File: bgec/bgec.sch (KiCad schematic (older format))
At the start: 7 parts

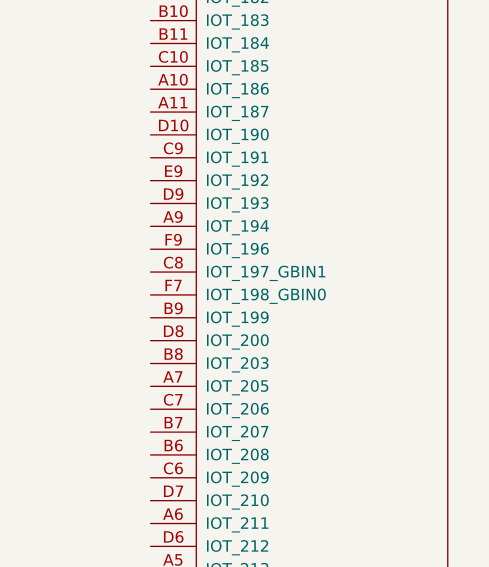
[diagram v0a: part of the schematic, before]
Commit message: Add clock and reset connections
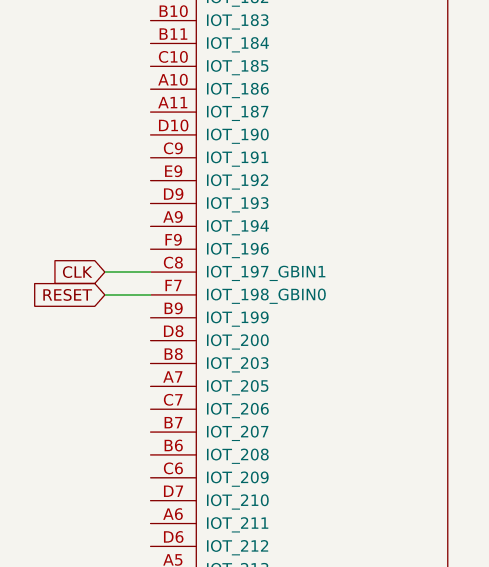
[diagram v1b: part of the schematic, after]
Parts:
- C1: footprint (none) -> Capacitor_SMD:C_0402_1005Metric
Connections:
- net CLK: now also FPGAiCE40HX1.C8 (IOT_197_GBIN1)
- net RESET: now reaches FPGAiCE40HX1.F7 (IOT_198_GBIN0)
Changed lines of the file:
@@
 F 0 "C1" V 7402 1100 50  0000 C CNN
 F 1 "100nF" V 7311 1100 50  0000 C CNN
-F 2 "" H 7188 950 50  0001 C CNN
+F 2 "Capacitor_SMD:C_0402_1005Metric" H 7188 950 50  0001 C CNN
 F 3 "~" H 7150 1100 50  0001 C CNN
 	1    7150 1100
@@
 Text GLabel 7500 1300 2    50   Input ~ 0
 GCLogicGround
+Text GLabel 800  4100 0    50   Input ~ 0
+RESET
+Text GLabel 800  4000 0    50   Input ~ 0
+CLK
+Wire Wire Line
+	800  4000 1000 4000
+Wire Wire Line
+	800  4100 1000 4100
 $EndSCHEMATC

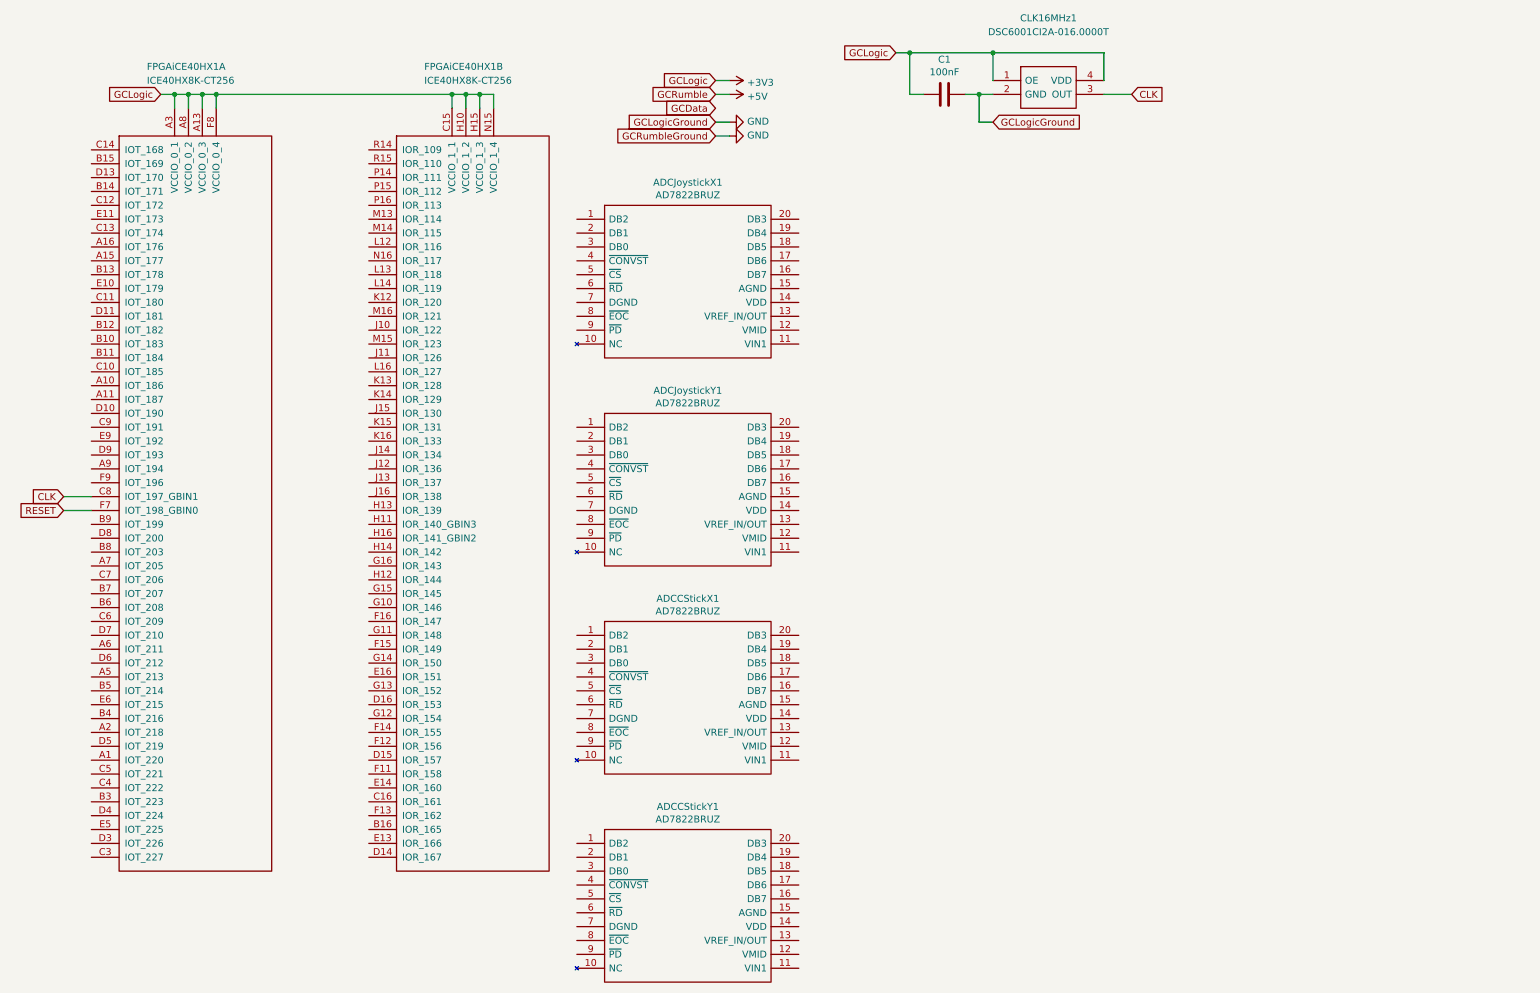
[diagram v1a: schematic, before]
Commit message: Connect the ADCs
I might be doing this wrong by ignoring CONVST. We'll see. I need to update the software side of things to start doing Parallel ADCs.
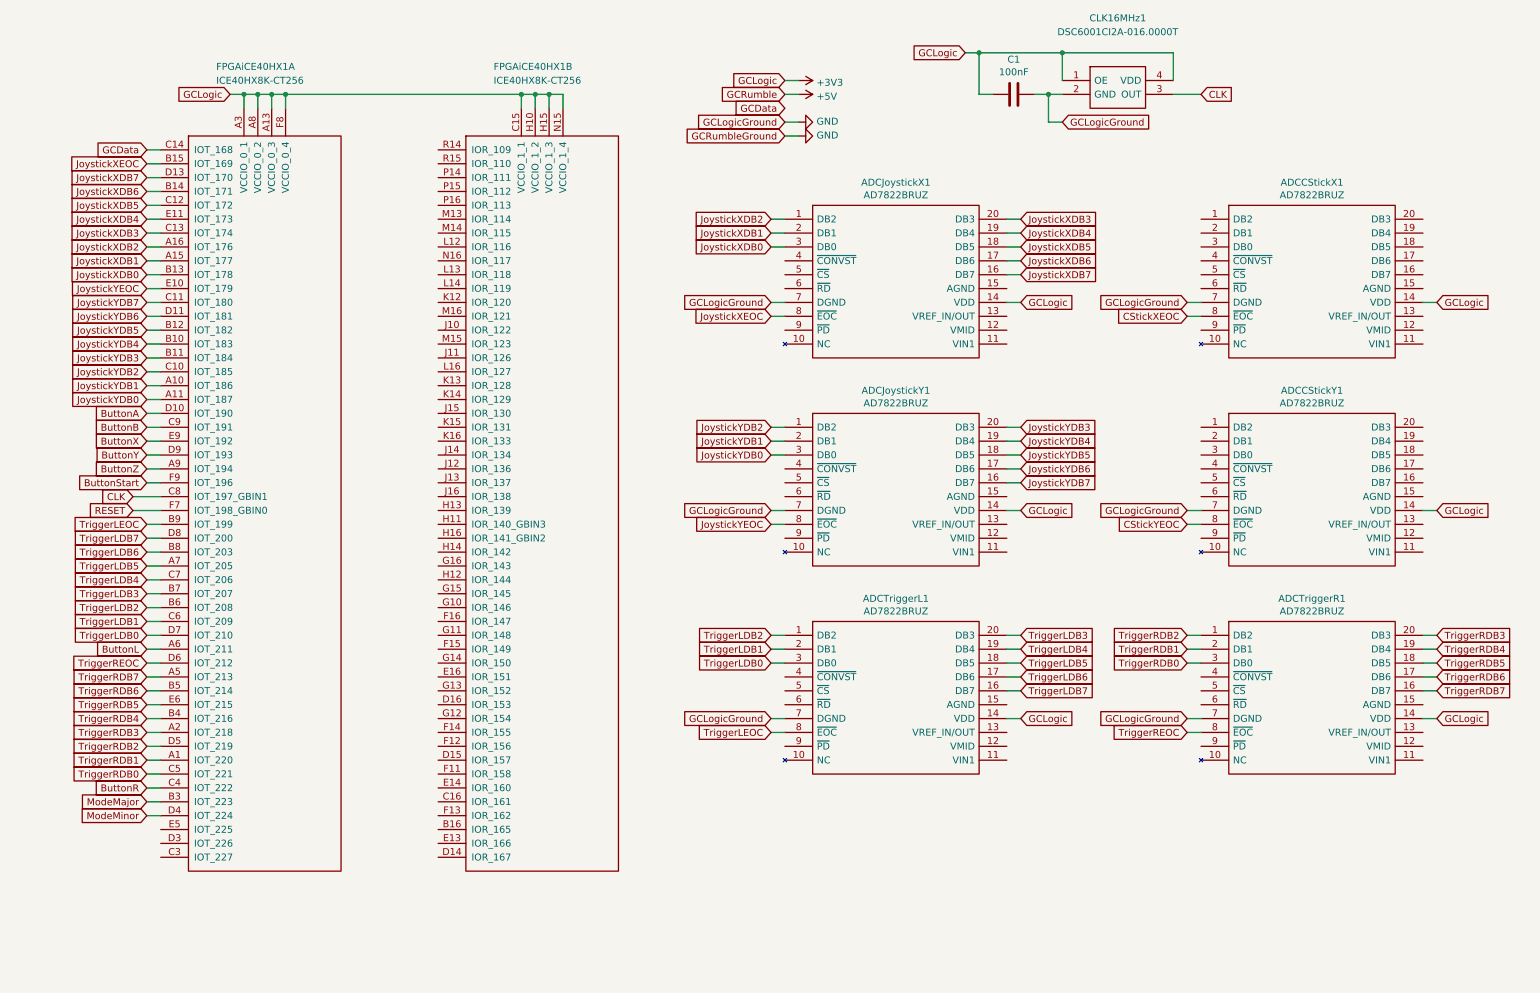
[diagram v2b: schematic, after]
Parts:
- added ADCTriggerL1, ADCTriggerR1: AD7822BRUZ, SOP65P640X120-20N, symbol bgec:AD7822BRUZ
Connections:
- net +3V3: now also ADCCStickX1.14 (VDD), ADCCStickY1.14 (VDD), ADCJoystickX1.14 (VDD), ADCJoystickY1.14 (VDD), ADCTriggerL1.14 (VDD), ADCTriggerR1.14 (VDD)
- net GCData: now also FPGAiCE40HX1.C14 (IOT_168)
- net GND: now also ADCCStickX1.7 (DGND), ADCCStickY1.7 (DGND), ADCJoystickX1.7 (DGND), ADCJoystickY1.7 (DGND), ADCTriggerL1.7 (DGND), ADCTriggerR1.7 (DGND)
- net JoystickXDB2: now reaches ADCJoystickX1.1 (DB2)
- net JoystickXDB2: now also FPGAiCE40HX1.A16 (IOT_176)
- net JoystickXDB7: now reaches ADCJoystickX1.16 (DB7)
- net JoystickXDB7: now also FPGAiCE40HX1.D13 (IOT_170)
- net JoystickXDB6: now reaches ADCJoystickX1.17 (DB6)
- net JoystickXDB6: now also FPGAiCE40HX1.B14 (IOT_171)
- net JoystickXDB5: now reaches ADCJoystickX1.18 (DB5)
- net JoystickXDB5: now also FPGAiCE40HX1.C12 (IOT_172)
- net JoystickXDB4: now reaches ADCJoystickX1.19 (DB4)
- net JoystickXDB4: now also FPGAiCE40HX1.E11 (IOT_173)
- net JoystickXDB1: now reaches ADCJoystickX1.2 (DB1)
- net JoystickXDB1: now also FPGAiCE40HX1.A15 (IOT_177)
- net JoystickXDB3: now reaches ADCJoystickX1.20 (DB3)
- net JoystickXDB3: now also FPGAiCE40HX1.C13 (IOT_174)
- net JoystickXDB0: now reaches ADCJoystickX1.3 (DB0)
- net JoystickXDB0: now also FPGAiCE40HX1.B13 (IOT_178)
- net JoystickXEOC: now reaches ADCJoystickX1.8 (~EOC)
- net JoystickXEOC: now also FPGAiCE40HX1.B15 (IOT_169)
- net JoystickYDB2: now reaches ADCJoystickY1.1 (DB2)
- net JoystickYDB2: now also FPGAiCE40HX1.C10 (IOT_185)
- net JoystickYDB7: now reaches ADCJoystickY1.16 (DB7)
- net JoystickYDB7: now also FPGAiCE40HX1.C11 (IOT_180)
- net JoystickYDB6: now reaches ADCJoystickY1.17 (DB6)
- net JoystickYDB6: now also FPGAiCE40HX1.D11 (IOT_181)
- net JoystickYDB5: now reaches ADCJoystickY1.18 (DB5)
- net JoystickYDB5: now also FPGAiCE40HX1.B12 (IOT_182)
- net JoystickYDB4: now reaches ADCJoystickY1.19 (DB4)
- net JoystickYDB4: now also FPGAiCE40HX1.B10 (IOT_183)
- net JoystickYDB1: now reaches ADCJoystickY1.2 (DB1)
- net JoystickYDB1: now also FPGAiCE40HX1.A10 (IOT_186)
- net JoystickYDB3: now reaches ADCJoystickY1.20 (DB3)
- net JoystickYDB3: now also FPGAiCE40HX1.B11 (IOT_184)
- net JoystickYDB0: now reaches ADCJoystickY1.3 (DB0)
- net JoystickYDB0: now also FPGAiCE40HX1.A11 (IOT_187)
- net JoystickYEOC: now reaches ADCJoystickY1.8 (~EOC)
- net JoystickYEOC: now also FPGAiCE40HX1.E10 (IOT_179)
- net CStickXEOC: now reaches ADCCStickX1.8 (~EOC)
- net CStickYEOC: now reaches ADCCStickY1.8 (~EOC)
- net TriggerRDB1: now reaches FPGAiCE40HX1.A1 (IOT_220)
- net TriggerRDB1: now also ADCTriggerR1.2 (DB1)
- net TriggerRDB3: now reaches FPGAiCE40HX1.A2 (IOT_218)
- net TriggerRDB3: now also ADCTriggerR1.20 (DB3)
- net TriggerRDB7: now reaches FPGAiCE40HX1.A5 (IOT_213)
- net TriggerRDB7: now also ADCTriggerR1.16 (DB7)
- net ButtonL: now reaches FPGAiCE40HX1.A6 (IOT_211)
- net TriggerLDB5: now reaches FPGAiCE40HX1.A7 (IOT_205)
- net TriggerLDB5: now also ADCTriggerL1.18 (DB5)
- net ButtonZ: now reaches FPGAiCE40HX1.A9 (IOT_194)
- net ModeMajor: now reaches FPGAiCE40HX1.B3 (IOT_223)
- net TriggerRDB4: now reaches FPGAiCE40HX1.B4 (IOT_216)
- net TriggerRDB4: now also ADCTriggerR1.19 (DB4)
- net TriggerRDB6: now reaches FPGAiCE40HX1.B5 (IOT_214)
- net TriggerRDB6: now also ADCTriggerR1.17 (DB6)
- net TriggerLDB2: now reaches FPGAiCE40HX1.B6 (IOT_208)
- net TriggerLDB2: now also ADCTriggerL1.1 (DB2)
- net TriggerLDB3: now reaches FPGAiCE40HX1.B7 (IOT_207)
- net TriggerLDB3: now also ADCTriggerL1.20 (DB3)
- net TriggerLDB6: now reaches FPGAiCE40HX1.B8 (IOT_203)
- net TriggerLDB6: now also ADCTriggerL1.17 (DB6)
- net TriggerLEOC: now reaches FPGAiCE40HX1.B9 (IOT_199)
- net TriggerLEOC: now also ADCTriggerL1.8 (~EOC)
- net ButtonR: now reaches FPGAiCE40HX1.C4 (IOT_222)
- net TriggerRDB0: now reaches FPGAiCE40HX1.C5 (IOT_221)
- net TriggerRDB0: now also ADCTriggerR1.3 (DB0)
- net TriggerLDB1: now reaches FPGAiCE40HX1.C6 (IOT_209)
- net TriggerLDB1: now also ADCTriggerL1.2 (DB1)
- net TriggerLDB4: now reaches FPGAiCE40HX1.C7 (IOT_206)
- net TriggerLDB4: now also ADCTriggerL1.19 (DB4)
- net ButtonB: now reaches FPGAiCE40HX1.C9 (IOT_191)
- net ButtonA: now reaches FPGAiCE40HX1.D10 (IOT_190)
- net ModeMinor: now reaches FPGAiCE40HX1.D4 (IOT_224)
- net TriggerRDB2: now reaches FPGAiCE40HX1.D5 (IOT_219)
- net TriggerRDB2: now also ADCTriggerR1.1 (DB2)
- net TriggerREOC: now reaches FPGAiCE40HX1.D6 (IOT_212)
- net TriggerREOC: now also ADCTriggerR1.8 (~EOC)
- net TriggerLDB0: now reaches FPGAiCE40HX1.D7 (IOT_210)
- net TriggerLDB0: now also ADCTriggerL1.3 (DB0)
- net TriggerLDB7: now reaches FPGAiCE40HX1.D8 (IOT_200)
- net TriggerLDB7: now also ADCTriggerL1.16 (DB7)
- net ButtonY: now reaches FPGAiCE40HX1.D9 (IOT_193)
- net TriggerRDB5: now reaches FPGAiCE40HX1.E6 (IOT_215)
- net TriggerRDB5: now also ADCTriggerR1.18 (DB5)
- net ButtonX: now reaches FPGAiCE40HX1.E9 (IOT_192)
- net ButtonStart: now reaches FPGAiCE40HX1.F9 (IOT_196)
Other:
- moved on the sheet: ADCCStickX1, ADCCStickY1, ADCJoystickX1, ADCJoystickY1, C1, CLK16MHz1, FPGAiCE40HX1A, FPGAiCE40HX1B

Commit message: Split into multiple sheets
Next problem to solve is routing. KiCad and Freerouter really hate that FPGA.
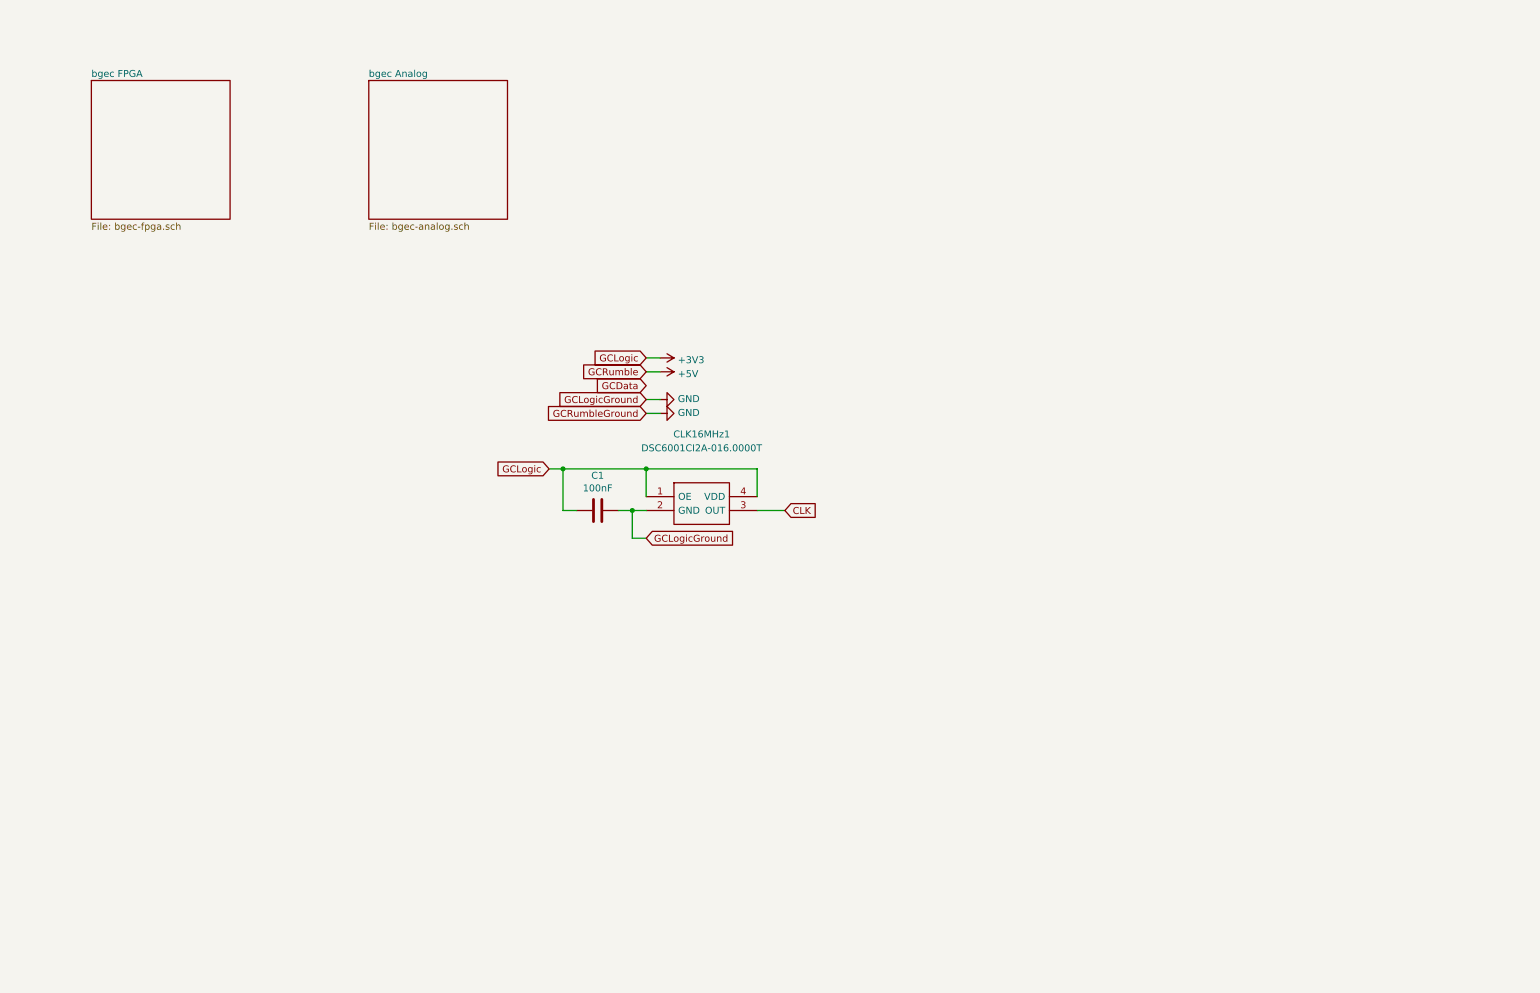
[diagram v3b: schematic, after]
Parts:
- removed ADCCStickX1, ADCCStickY1, ADCJoystickX1, ADCJoystickY1, ADCTriggerL1, ADCTriggerR1: AD7822BRUZ, SOP65P640X120-20N, symbol bgec:AD7822BRUZ
- removed FPGAiCE40HX1: ICE40HX8K-CT256, bgec:BGA256C80P16X16_1400X1400X170, symbol bgec:ICE40HX8K-CT256
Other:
- moved on the sheet: C1, CLK16MHz1

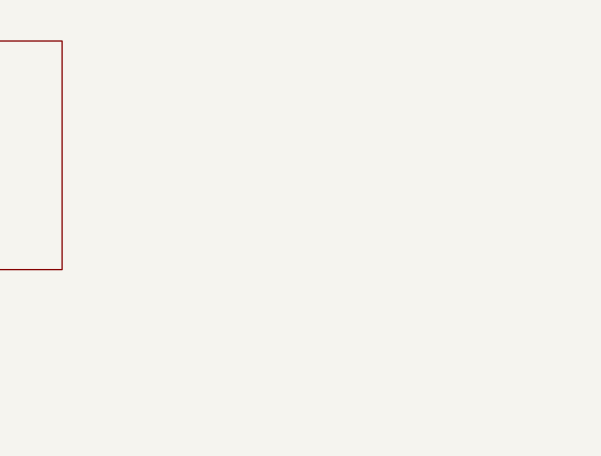
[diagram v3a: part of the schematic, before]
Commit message: Remodel ADC placement, add USB-C connector
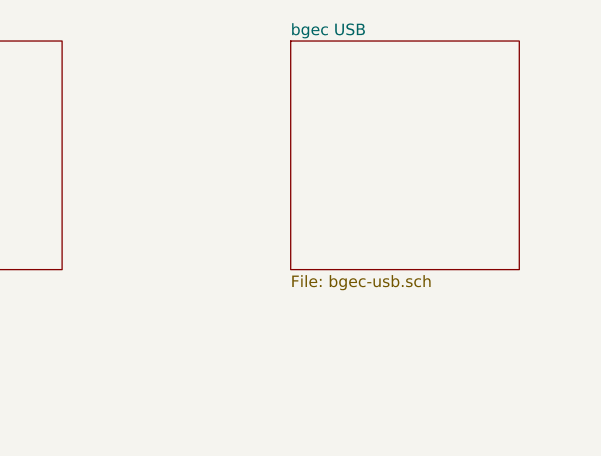
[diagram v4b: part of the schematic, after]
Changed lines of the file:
@@
 $Descr A4 11693 8268
 encoding utf-8
-Sheet 1 3
+Sheet 1 4
 Title "bgec"
 Date "2020-02-19"
@@
 Text GLabel 5000 4300 2    50   Input ~ 0
 GCLogicGround
+$Sheet
+S 5000 1000 1000 1000
+U 5E5D99D4
+F0 "bgec USB" 50
+F1 "bgec-usb.sch" 50
+$EndSheet
 $EndSCHEMATC
